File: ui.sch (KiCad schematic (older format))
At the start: 45 parts, among them SW1 SW_Push, SW2 SW_Push, SW3 SW_Push, SW4 SW_Push, SW5 SW_Push, SW8 JS202011SCQN, SW9 JS202011SCQN, U1 ICE40HX4K-TQ144

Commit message: ui sheet
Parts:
- removed U1: ICE40HX4K-TQ144, symbol ice40hx4k:ICE40HX4K-TQ144
- renumbered C21 to C?, C22 to C?, C23 to C?, C24 to C?, C25 to C?, C42 to C?, C74 to C?, D1 to D?, D2 to D?, D3 to D?, D4 to D?, D5 to D?, D6 to D?, D7 to D?, D8 to D?, R1 to R?, R2 to R?, R3 to R?, R4 to R?, R5 to R?, R6 to R?, R7 to R?, R8 to R?, R9 to R?, R10 to R?, R11 to R?, R12 to R?, R13 to R?, R24 to R?, R25 to R?, R26 to R?, R27 to R?, R28 to R?, R50 to R?, R56 to R?, R51 to R?, R57 to R?, SW1 to SW?, SW2 to SW?, SW3 to SW?, SW4 to SW?, SW5 to SW?
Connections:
- no-connect marks 9 -> 8
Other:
- moved on the sheet: C?, D?, R?, SW?

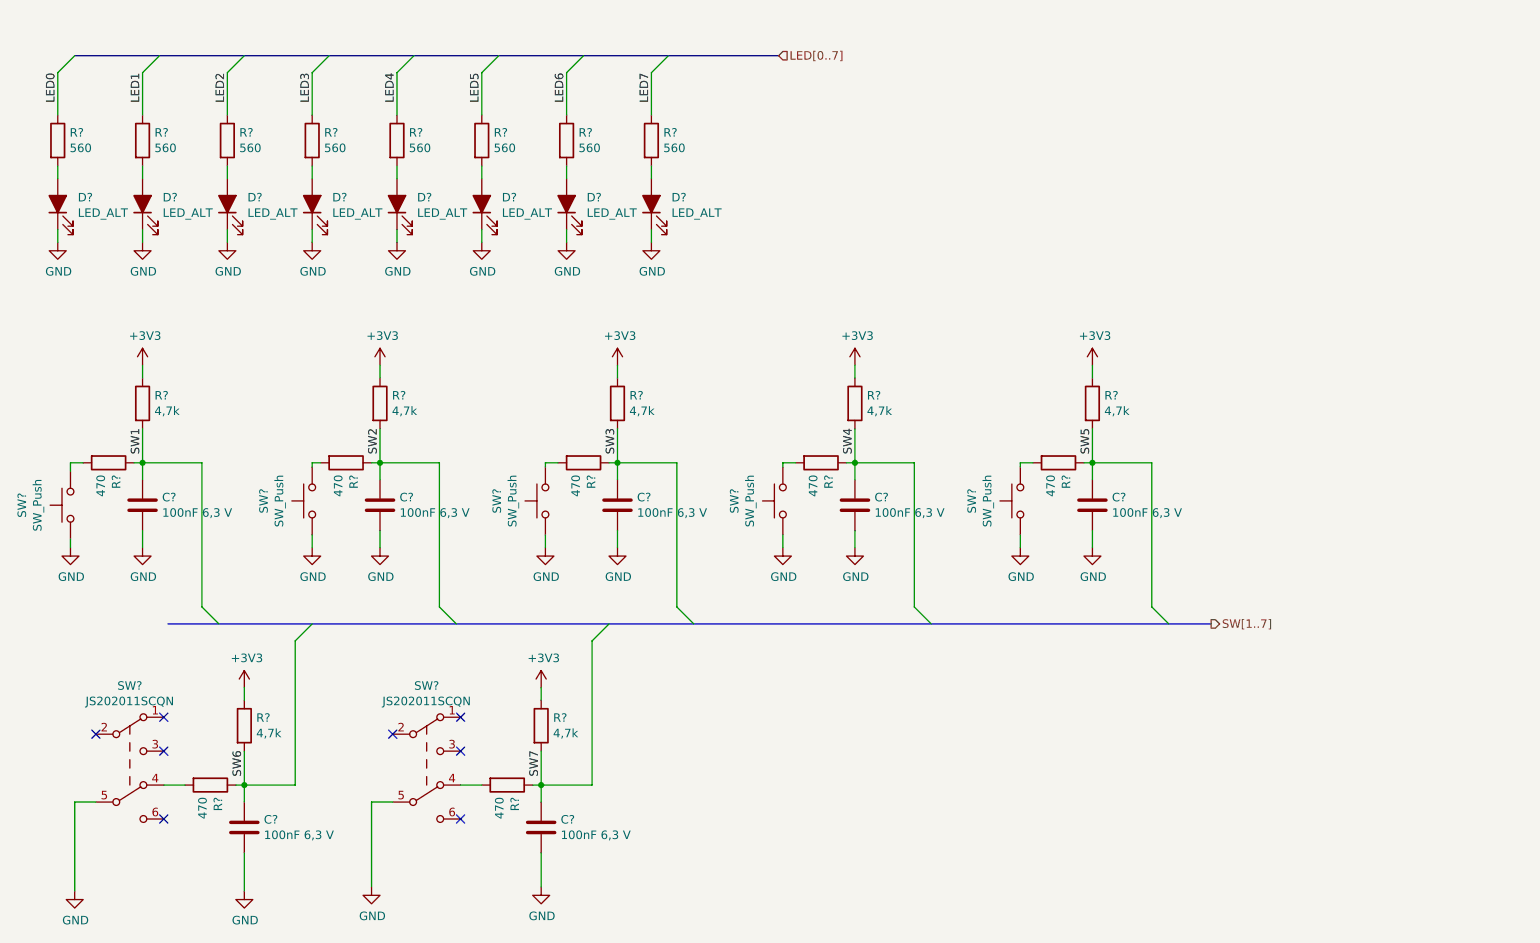
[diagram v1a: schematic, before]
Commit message: Schematic modified (Hierarchy) Bug where SPI was active when creset or ss was low fixed PCB layout started (almost all parts are at position) No parts on the bottom so far Arduino and PMOD header spacings corrected according to its standards
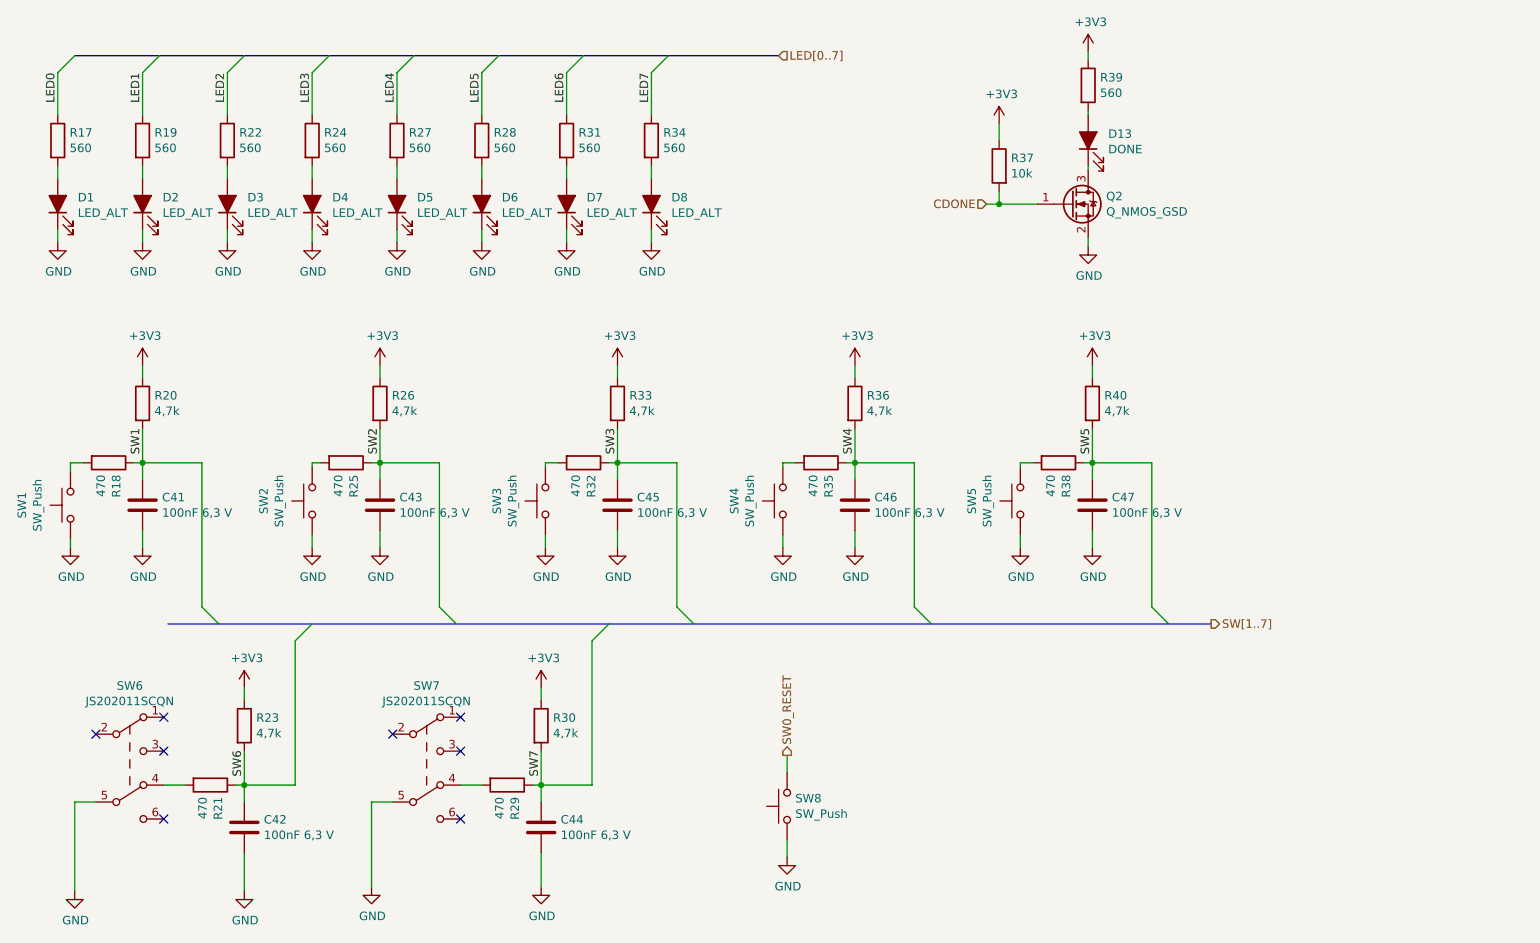
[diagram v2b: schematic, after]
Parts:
- added D13: DONE, LED_SMD:LED_0603_1608Metric, symbol Device:LED_ALT
- added Q2: Q_NMOS_GSD, Package_TO_SOT_SMD:SOT-23, symbol Device:Q_NMOS_GSD
- added R37: 10k, Resistor_SMD:R_0603_1608Metric, symbol Device:R
- added R39: 560, Resistor_SMD:R_0603_1608Metric, symbol Device:R
- added SW8: SW_Push, footprints:SW_SPST_TL3305A, symbol Switch:SW_Push
- gave numbers to parts that had none: 42
- renumbered SW8 to SW6, SW9 to SW7
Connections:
- net +3V3: now also R37.1, R39.1
- net GND: now also Q2.2 (S), SW8.1
- new net: D13.1 (K), Q2.3 (D)
- new net: D13.2 (A), R39.2
- new net CDONE: Q2.1 (G), R37.2
- new net SW0_RESET: SW8.2
